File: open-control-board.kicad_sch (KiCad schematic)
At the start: 155 parts, among them CN1 LCC Port, CN14 Conn_02x06_Odd_Even, CN2 Conn_01x06_Pin, CN3 12V Separate Supply, CN4 Conn_02x05_Counter_Clockwise, CN5 NTC Brew Boiler, CN6 NTC Service Boiler, CN7 Conn_01x06_Pin, CN8 Conn_01x05_Pin, CN9 Conn_02x04_Counter_Clockwise, J1 USB_B_Micro, J13 Conn_02x05_Odd_Even, J15 Conn_02x05_Odd_Even, J16 USB_B_Micro, J3 Conn_02x03_Odd_Even, J5 BM04B-SRSS-TB(LF)(SN), Q1 AO3401A, Q11 DMN63D8LDW, Q2 AO3401A, Q3 Q_PMOS-E_DUAL_Generic_SEP_S1G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, Q4 DMN63D8LDW, Q5 Q_PMOS-E_DUAL_Generic_SEP_S1G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, Q6 DMN63D8LDW, Q7 DMN63D8LDW, SW1 SW_Push, SW2 SW_Push, SW3 SW_Push, SW4 SW_Push, U10 FDC1004, U11 ADS1115IDGS, U12 ADS1115IDGS, U15 STPIC6C595TTR, U16 STPIC6C595TTR, U2 RP2040, U3 ESP32-S3-WROOM-1, U4 W25Q16JVUXIQ, U6 TPS82130, U7 TXS0108EPWR, U8 TXS0108EPWR, Y1 XYDBPCNANF-12MHZ

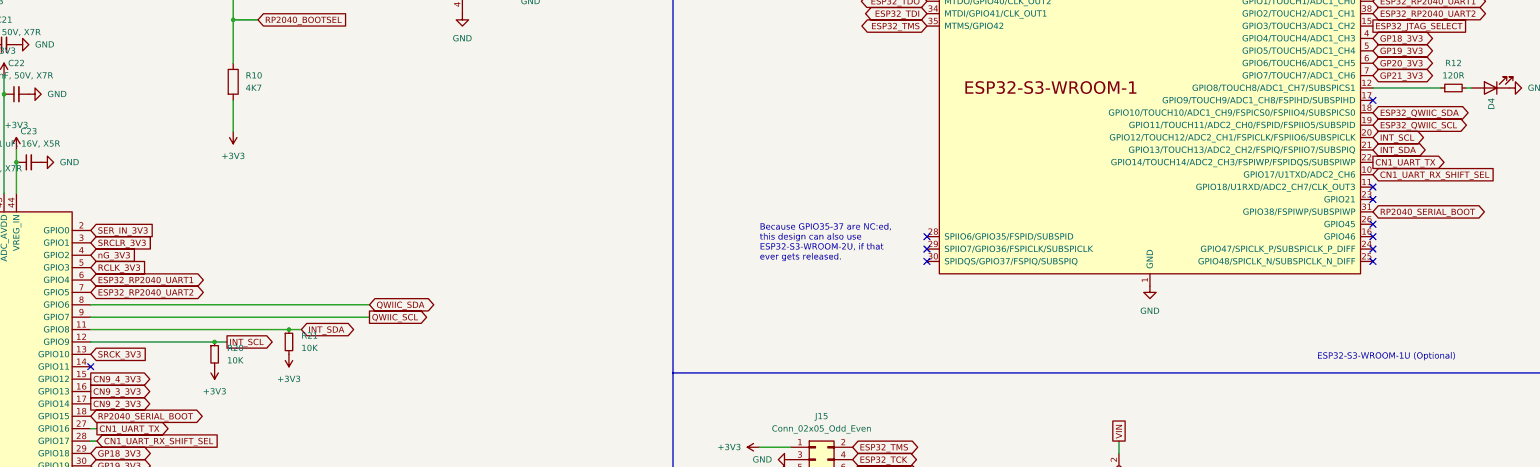
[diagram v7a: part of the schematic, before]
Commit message: Added test points for unused IO
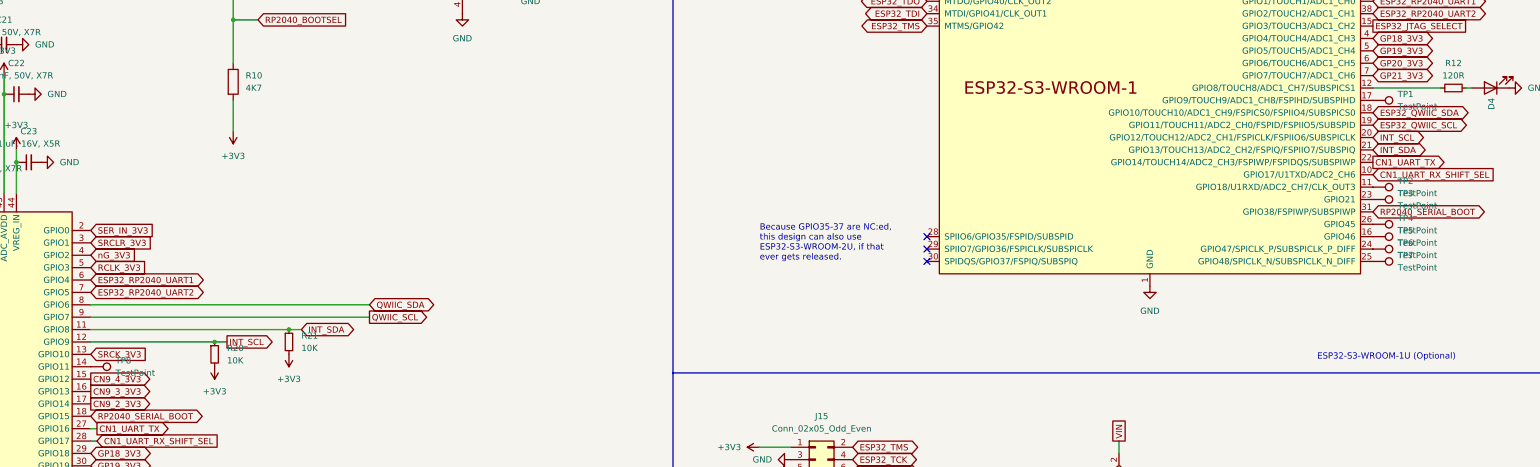
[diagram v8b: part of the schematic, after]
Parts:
- added TP1, TP2, TP3, TP4, TP5, TP6, TP7, TP8: TestPoint, TestPoint:TestPoint_Pad_D1.0mm, symbol Connector:TestPoint
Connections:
- net at U3.11 (GPIO18/U1RXD/ADC2_CH7/CLK_OUT3): now also TP2.1
- net at U3.16 (GPIO46): now also TP5.1
- net at U3.17 (GPIO9/TOUCH9/ADC1_CH8/FSPIHD/SUBSPIHD): now also TP1.1
- net at U3.23 (GPIO21): now also TP3.1
- net at U3.24 (GPIO47/SPICLK_P/SUBSPICLK_P_DIFF): now also TP6.1
- net at U3.25 (GPIO48/SPICLK_N/SUBSPICLK_N_DIFF): now also TP7.1
- net at U3.26 (GPIO45): now also TP4.1
- net at U2.14 (GPIO11): now also TP8.1
- no-connect marks 25 -> 17
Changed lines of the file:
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@@
   (junction (at 613.41 311.15) (diameter 0) (color 0 0 0 0)
   )
-  (no_connect (at 615.95 118.11))
-  (no_connect (at 615.95 115.57))
-  (no_connect (at 207.01 401.32))
+  (no_connect (at 209.55 401.32))
   (no_connect (at 161.29 93.98))
+  (no_connect (at 207.01 401.32))
+  (no_connect (at 207.01 374.65))
   (no_connect (at 38.1 273.05))
-  (no_connect (at 209.55 401.32))
-  (no_connect (at 615.95 120.65))
   (no_connect (at 524.51 115.57))
+  (no_connect (at 209.55 374.65))
   (no_connect (at 561.34 184.15))
-  (no_connect (at 207.01 374.65))
-  (no_connect (at 615.95 105.41))
   (no_connect (at 43.18 226.06))
-  (no_connect (at 209.55 374.65))
-  (no_connect (at 615.95 87.63))
   (no_connect (at 43.18 223.52))
   (no_connect (at 496.57 166.37))
   (no_connect (at 524.51 120.65))
-  (no_connect (at 615.95 107.95))
   (no_connect (at 524.51 118.11))
   (no_connect (at 187.96 152.4))
-  (no_connect (at 615.95 113.03))
-  (no_connect (at 353.06 142.24))
   (no_connect (at 187.96 223.52))
   (no_connect (at 30.48 226.06))
@@
     )
   )
+  (symbol (lib_id "Connector:TestPoint") (at 615.95 113.03 270) (unit 1)
+    (in_bom yes) (on_board yes) (dnp no) (fields_autoplaced)
+    (property "Reference" "TP4" (at 621.03 111.76 90)
+      (effects (font (size 1.27 1.27)) (justify left))
+    )
+    (property "Value" "TestPoint" (at 621.03 114.3 90)
+      (effects (font (size 1.27 1.27)) (justify left))
+    )
+    (property "Footprint" "TestPoint:TestPoint_Pad_D1.0mm" (at 615.95 118.11 0)
+      (effects (font (size 1.27 1.27)) hide)
+    )
+    (property "Datasheet" "~" (at 615.95 118.11 0)
+      (effects (font (size 1.27 1.27)) hide)
+    )
+    (pin "1")
+    (instances
+      (project "open-control-board"
+        (path "/c7c8c763-88fa-419b-8f4a-ebade330cc39"
+          (reference "TP4") (unit 1)
+        )
+      )
+    )
+  )
   (symbol (lib_id "Device:R_Small") (at 181.61 403.86 270) (unit 1)
     (in_bom yes) (on_board yes) (dnp no) (fields_autoplaced)
@@
     )
   )
+  (symbol (lib_id "Connector:TestPoint") (at 615.95 115.57 270) (unit 1)
+    (in_bom yes) (on_board yes) (dnp no) (fields_autoplaced)
+    (property "Reference" "TP5" (at 621.03 114.3 90)
+      (effects (font (size 1.27 1.27)) (justify left))
+    )
+    (property "Value" "TestPoint" (at 621.03 116.84 90)
+      (effects (font (size 1.27 1.27)) (justify left))
+    )
+    (property "Footprint" "TestPoint:TestPoint_Pad_D1.0mm" (at 615.95 120.65 0)
+      (effects (font (size 1.27 1.27)) hide)
+    )
+    (property "Datasheet" "~" (at 615.95 120.65 0)
+      (effects (font (size 1.27 1.27)) hide)
+    )
+    (pin "1")
+    (instances
+      (project "open-control-board"
+        (path "/c7c8c763-88fa-419b-8f4a-ebade330cc39"
+          (reference "TP5") (unit 1)
+        )
+      )
+    )
+  )
   (symbol (lib_id "PCM_Transistor_MOSFET_AKL:DMN63D8LDW") (at 327.66 345.44 270) (unit 2)
     (in_bom yes) (on_board yes) (dnp no)
@@
     )
   )
+  (symbol (lib_id "Connector:TestPoint") (at 615.95 87.63 270) (unit 1)
+    (in_bom yes) (on_board yes) (dnp no) (fields_autoplaced)
+    (property "Reference" "TP1" (at 621.03 86.36 90)
+      (effects (font (size 1.27 1.27)) (justify left))
+    )
+    (property "Value" "TestPoint" (at 621.03 88.9 90)
+      (effects (font (size 1.27 1.27)) (justify left))
+    )
+    (property "Footprint" "TestPoint:TestPoint_Pad_D1.0mm" (at 615.95 92.71 0)
+      (effects (font (size 1.27 1.27)) hide)
+    )
+    (property "Datasheet" "~" (at 615.95 92.71 0)
+      (effects (font (size 1.27 1.27)) hide)
+    )
+    (pin "1")
+    (instances
+      (project "open-control-board"
+        (path "/c7c8c763-88fa-419b-8f4a-ebade330cc39"
+          (reference "TP1") (unit 1)
+        )
+      )
+    )
+  )
   (symbol (lib_id "PCM_Transistor_MOSFET_AKL:DMN63D8LDW") (at 166.37 326.39 90) (mirror x) (unit 2)
     (in_bom yes) (on_board yes) (dnp no)
@@
     )
   )
+  (symbol (lib_id "Connector:TestPoint") (at 615.95 118.11 270) (unit 1)
+    (in_bom yes) (on_board yes) (dnp no) (fields_autoplaced)
+    (property "Reference" "TP6" (at 621.03 116.84 90)
+      (effects (font (size 1.27 1.27)) (justify left))
+    )
+    (property "Value" "TestPoint" (at 621.03 119.38 90)
+      (effects (font (size 1.27 1.27)) (justify left))
+    )
+    (property "Footprint" "TestPoint:TestPoint_Pad_D1.0mm" (at 615.95 123.19 0)
+      (effects (font (size 1.27 1.27)) hide)
+    )
+    (property "Datasheet" "~" (at 615.95 123.19 0)
+      (effects (font (size 1.27 1.27)) hide)
+    )
+    (pin "1")
+    (instances
+      (project "open-control-board"
+        (path "/c7c8c763-88fa-419b-8f4a-ebade330cc39"
+          (reference "TP6") (unit 1)
+        )
+      )
+    )
+  )
   (symbol (lib_id "power:GND") (at 204.47 77.47 90) (unit 1)
     (in_bom yes) (on_board yes) (dnp no) (fields_autoplaced)
@@
     )
   )
+  (symbol (lib_id "Connector:TestPoint") (at 615.95 105.41 270) (unit 1)
+    (in_bom yes) (on_board yes) (dnp no) (fields_autoplaced)
+    (property "Reference" "TP2" (at 621.03 104.14 90)
+      (effects (font (size 1.27 1.27)) (justify left))
+    )
+    (property "Value" "TestPoint" (at 621.03 106.68 90)
+      (effects (font (size 1.27 1.27)) (justify left))
+    )
+    (property "Footprint" "TestPoint:TestPoint_Pad_D1.0mm" (at 615.95 110.49 0)
+      (effects (font (size 1.27 1.27)) hide)
+    )
+    (property "Datasheet" "~" (at 615.95 110.49 0)
+      (effects (font (size 1.27 1.27)) hide)
+    )
+    (pin "1")
+    (instances
+      (project "open-control-board"
+        (path "/c7c8c763-88fa-419b-8f4a-ebade330cc39"
+          (reference "TP2") (unit 1)
+        )
+      )
+    )
+  )
   (symbol (lib_id "power:+3V3") (at 269.24 307.34 0) (unit 1)
     (in_bom yes) (on_board yes) (dnp no) (fields_autoplaced)
@@
     )
   )
+  (symbol (lib_id "Connector:TestPoint") (at 353.06 142.24 270) (unit 1)
+    (in_bom yes) (on_board yes) (dnp no) (fields_autoplaced)
+    (property "Reference" "TP8" (at 358.14 140.97 90)
+      (effects (font (size 1.27 1.27)) (justify left))
+    )
+    (property "Value" "TestPoint" (at 358.14 143.51 90)
+      (effects (font (size 1.27 1.27)) (justify left))
+    )
+    (property "Footprint" "TestPoint:TestPoint_Pad_D1.0mm" (at 353.06 147.32 0)
+      (effects (font (size 1.27 1.27)) hide)
+    )
+    (property "Datasheet" "~" (at 353.06 147.32 0)
+      (effects (font (size 1.27 1.27)) hide)
+    )
+    (pin "1")
+    (instances
+      (project "open-control-board"
+        (path "/c7c8c763-88fa-419b-8f4a-ebade330cc39"
+          (reference "TP8") (unit 1)
+        )
+      )
+    )
+  )
   (symbol (lib_id "power:GND") (at 443.23 62.23 0) (unit 1)
     (in_bom yes) (on_board yes) (dnp no) (fields_autoplaced)
@@
     )
   )
+  (symbol (lib_id "Connector:TestPoint") (at 615.95 120.65 270) (unit 1)
+    (in_bom yes) (on_board yes) (dnp no) (fields_autoplaced)
+    (property "Reference" "TP7" (at 621.03 119.38 90)
+      (effects (font (size 1.27 1.27)) (justify left))
+    )
+    (property "Value" "TestPoint" (at 621.03 121.92 90)
+      (effects (font (size 1.27 1.27)) (justify left))
+    )
+    (property "Footprint" "TestPoint:TestPoint_Pad_D1.0mm" (at 615.95 125.73 0)
+      (effects (font (size 1.27 1.27)) hide)
+    )
+    (property "Datasheet" "~" (at 615.95 125.73 0)
+      (effects (font (size 1.27 1.27)) hide)
+    )
+    (pin "1")
+    (instances
+      (project "open-control-board"
+        (path "/c7c8c763-88fa-419b-8f4a-ebade330cc39"
+          (reference "TP7") (unit 1)
+        )
+      )
+    )
+  )
   (symbol (lib_id "power:GND") (at 187.96 170.18 0) (unit 1)
     (in_bom yes) (on_board yes) (dnp no) (fields_autoplaced)
@@
         )
       )
+    )
+  )
+  (symbol (lib_id "Connector:TestPoint") (at 615.95 107.95 270) (unit 1)
+    (in_bom yes) (on_board yes) (dnp no) (fields_autoplaced)
+    (property "Reference" "TP3" (at 621.03 106.68 90)
+      (effects (font (size 1.27 1.27)) (justify left))
+    )
+    (property "Value" "TestPoint" (at 621.03 109.22 90)
+      (effects (font (size 1.27 1.27)) (justify left))
+    )
+    (property "Footprint" "TestPoint:TestPoint_Pad_D1.0mm" (at 615.95 113.03 0)
+      (effects (font (size 1.27 1.27)) hide)
+    )
+    (property "Datasheet" "~" (at 615.95 113.03 0)
+      (effects (font (size 1.27 1.27)) hide)
+    )
+    (pin "1")
+    (instances
+      (project "open-control-board"
+        (path "/c7c8c763-88fa-419b-8f4a-ebade330cc39"
+          (reference "TP3") (unit 1)
+        )
+      )
